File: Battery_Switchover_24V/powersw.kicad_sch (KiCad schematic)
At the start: 22 parts, among them U4 LM74610QDGKRQ1, U5 FDBL86066-F085, U6 LM74610QDGKRQ1, U7 FDBL86066-F085

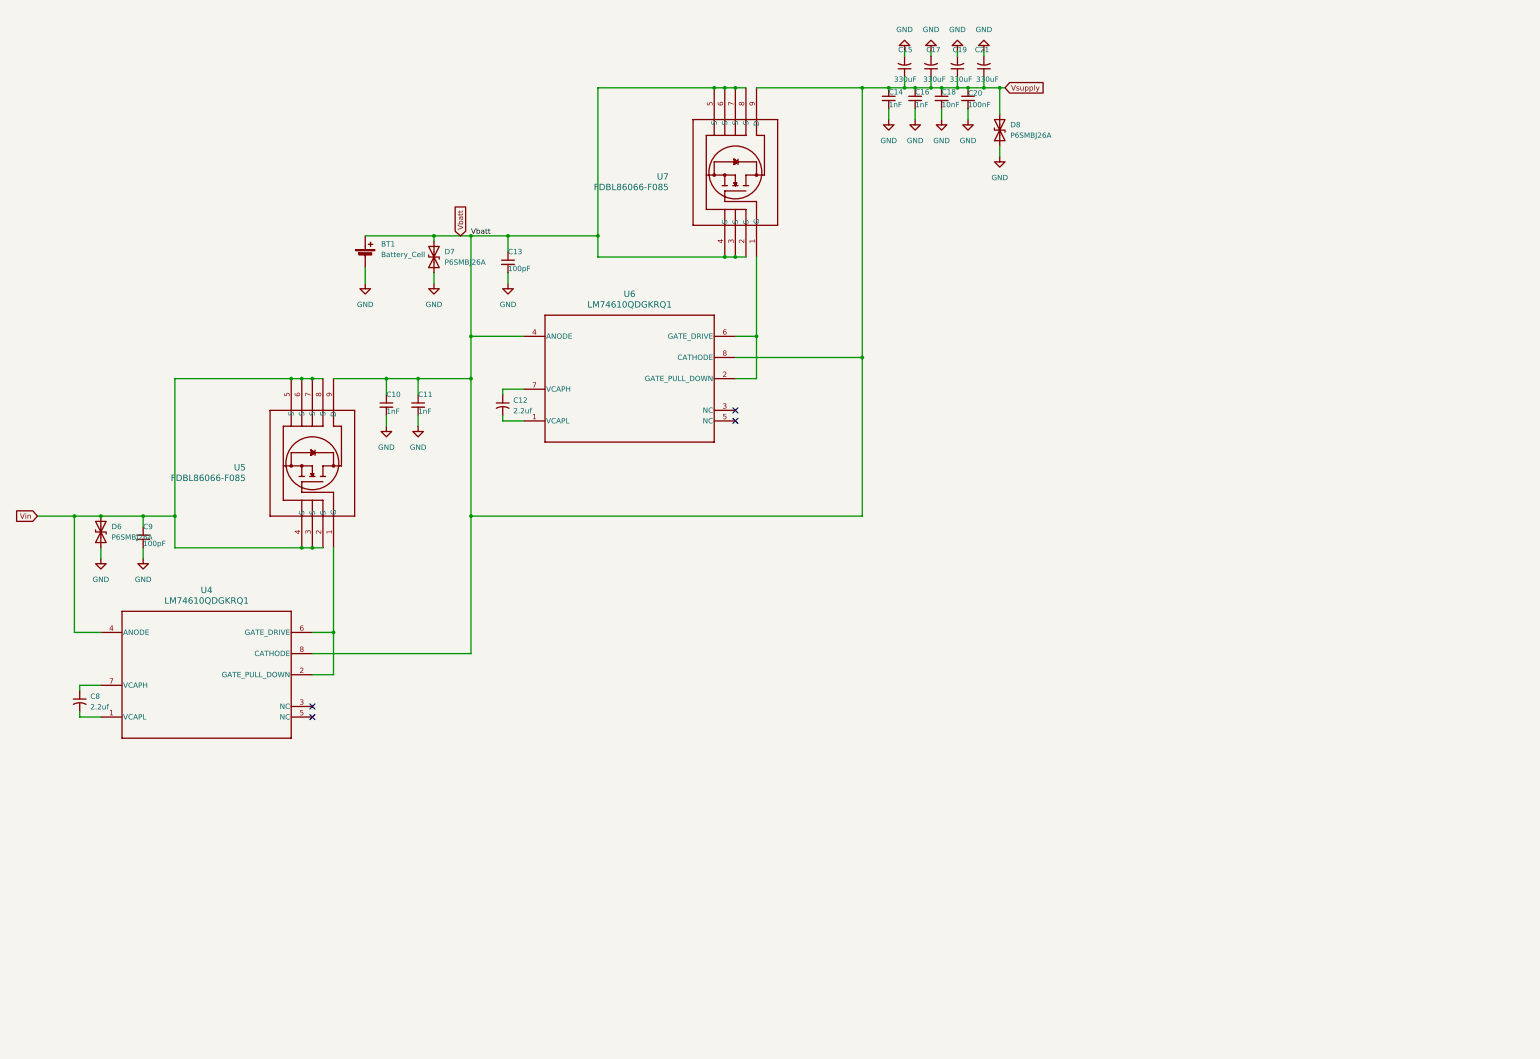
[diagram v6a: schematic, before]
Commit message: Added common mode chokes for input and output of the load fixed the corrupted board
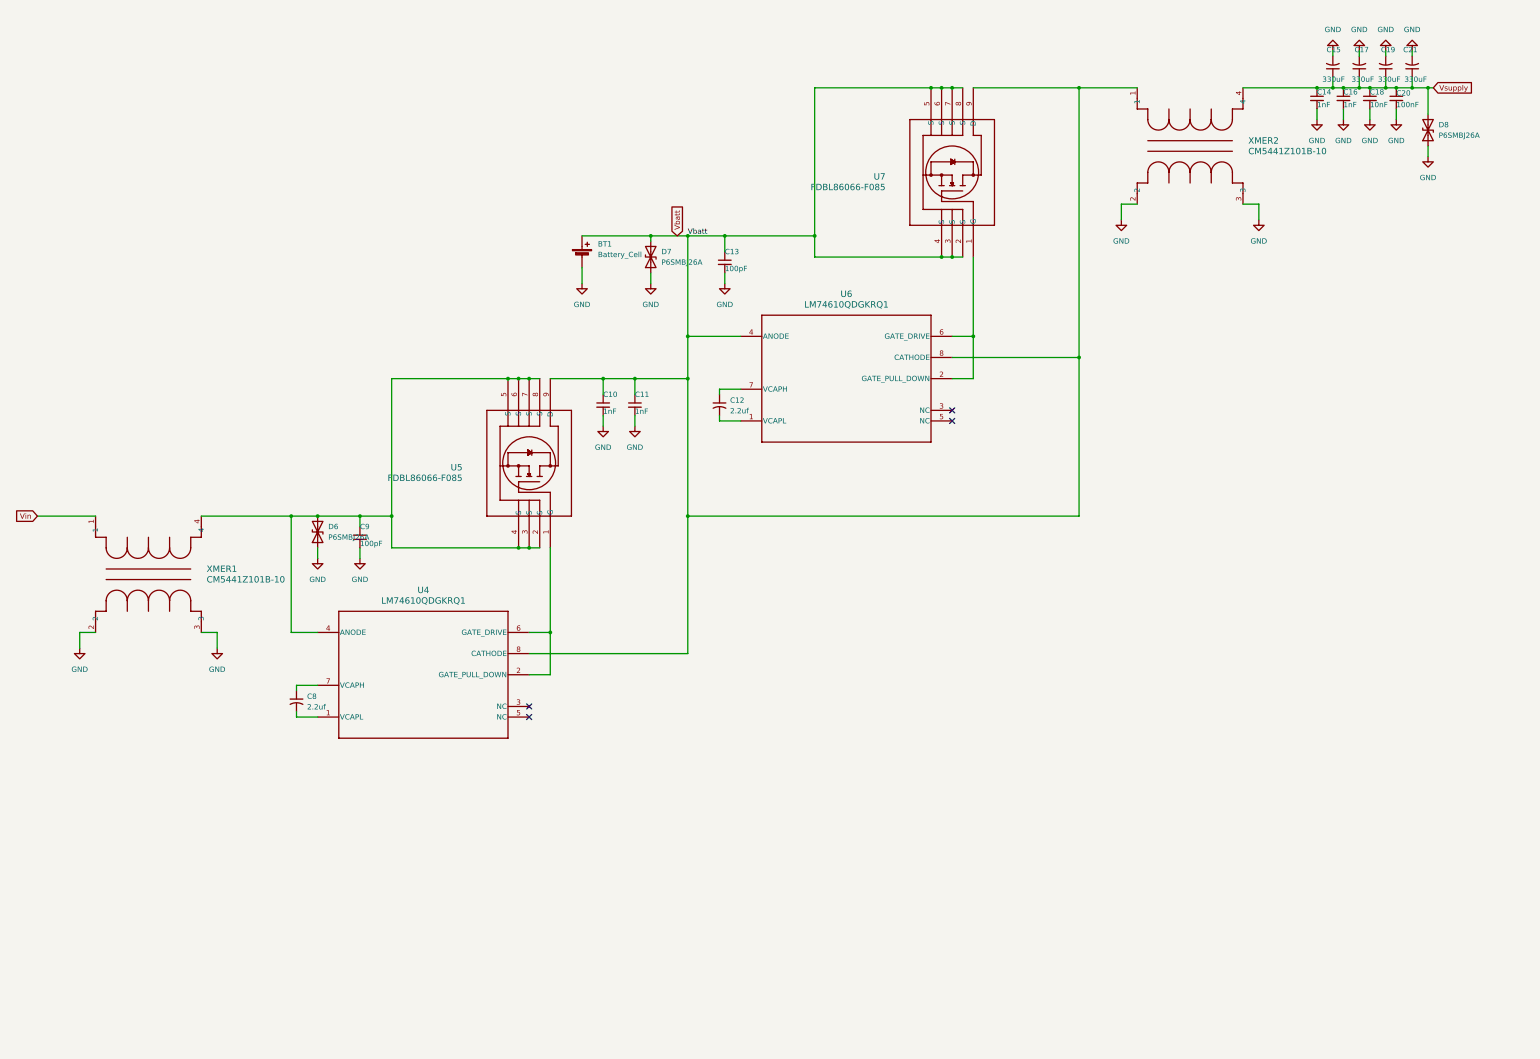
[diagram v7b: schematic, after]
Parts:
- added XMER1, XMER2: CM5441Z101B-10, footprints:CM5441Z101B-10_LRD, symbol CM5441Z161B-10:CM5441Z101B-10
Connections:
- net GND: now also XMER1.2, XMER1.3, XMER2.2, XMER2.3
- net Vbatt: now also XMER2.1; no longer C14.1, C15.1, C16.1, C17.1, C18.1, C19.1, C20.1, C21.1, D8.2 (A2)
- net Vin: now also XMER1.1; no longer C9.1, D6.2 (A2), U4.4 (ANODE), U5.2 (S), U5.3 (S), U5.4 (S), U5.5 (S), U5.6 (S), U5.7 (S), U5.8 (S)
- new net: C9.1, D6.2 (A2), U4.4 (ANODE), U5.2 (S), U5.3 (S), U5.4 (S), U5.5 (S), U5.6 (S), U5.7 (S), U5.8 (S), XMER1.4
- new net Vsupply: C14.1, C15.1, C16.1, C17.1, C18.1, C19.1, C20.1, C21.1, D8.2 (A2), XMER2.4
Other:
- moved on the sheet: BT1, C10, C11, C12, C13, C14, C15, C16, C17, C18, C19, C20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

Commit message: Added backup mosfets for protection
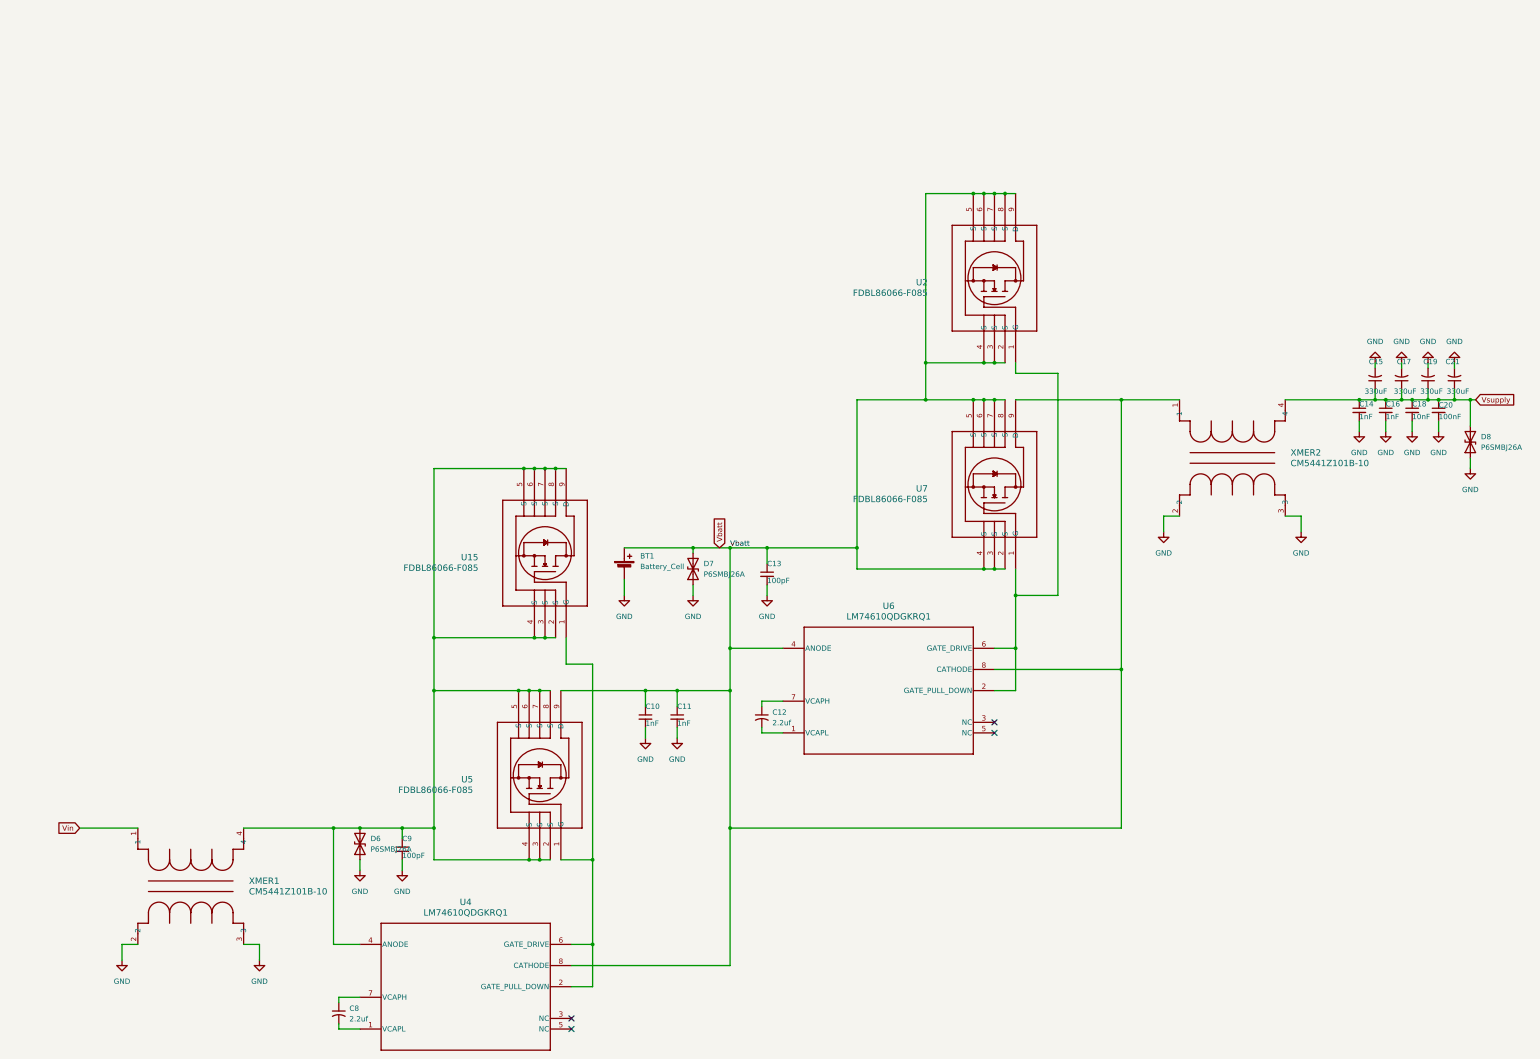
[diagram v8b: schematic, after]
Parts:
- added U15, U2: FDBL86066-F085, H-PSOF8L_ONS, symbol FDBL86062:FDBL86066-F085
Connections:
- net Vbatt: now also U2.2 (S), U2.3 (S), U2.4 (S), U2.5 (S), U2.6 (S), U2.7 (S), U2.8 (S), U2.9 (D)
- net at U6.2 (GATE_PULL_DOWN), U6.6 (GATE_DRIVE), U7.1 (G): now also U2.1 (G)
- net at U4.2 (GATE_PULL_DOWN), U4.6 (GATE_DRIVE), U5.1 (G): now also U15.1 (G)
- net at C9.1, D6.2 (A2), U4.4 (ANODE)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: now also U15.2 (S), U15.3 (S), U15.4 (S), U15.5 (S), U15.6 (S), U15.7 (S), U15.8 (S), U15.9 (D)
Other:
- moved on the sheet: BT1, C10, C11, C12, C13, C14, C15, C16, C17, C18, C19, C20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
